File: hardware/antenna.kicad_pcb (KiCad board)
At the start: 2 copper layers, 9 parts, among them P1 CONN_01X05

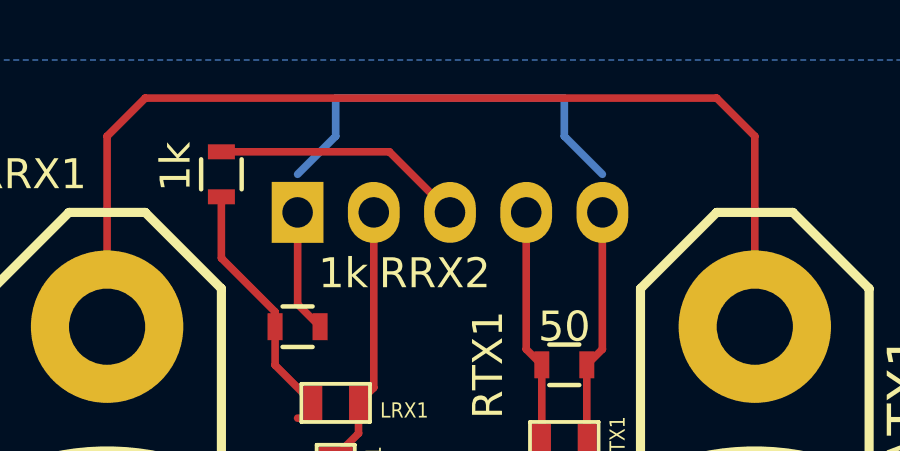
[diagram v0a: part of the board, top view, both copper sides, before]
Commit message: Fixing the ground plane fill.
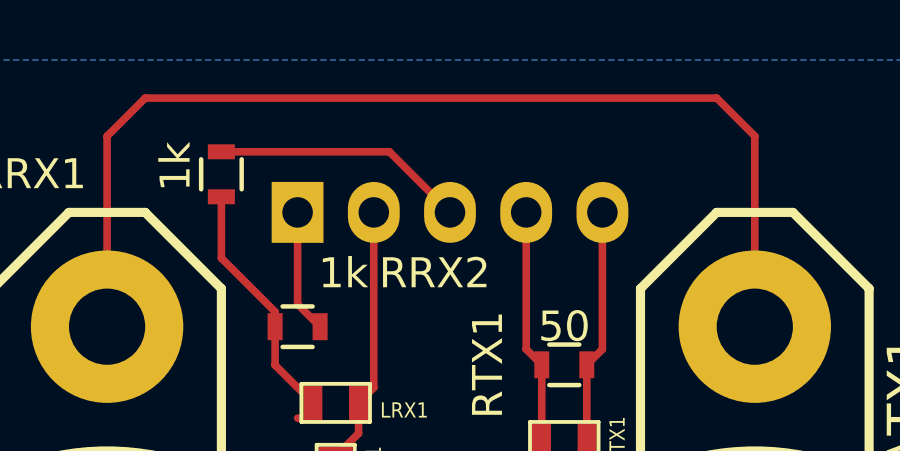
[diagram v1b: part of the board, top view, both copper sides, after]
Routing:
- net (no net): track 13.8 -> 0.00 mm
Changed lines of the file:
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@@
     (links 15)
     (no_connects 0)
-    (area 124.46 45.72 166.37 80.01)
+    (area 124.38608 45.72 165.100001 78.9432)
     (thickness 1.6)
     (drawings 0)
-    (tracks 37)
+    (tracks 32)
     (zones 0)
     (modules 9)
@@
     )
   )
-  (segment (start 139.7 49.53) (end 140.97 48.26) (width 0.254) (layer B.Cu) (net 0) (status 80010))
-  (segment (start 140.97 48.26) (end 140.97 46.99) (width 0.254) (layer B.Cu) (net 0) (status 80000))
-  (segment (start 140.97 46.99) (end 148.59 46.99) (width 0.254) (layer B.Cu) (net 0) (status 80000))
-  (segment (start 148.59 46.99) (end 148.59 48.26) (width 0.254) (layer B.Cu) (net 0) (status 80000))
-  (segment (start 148.59 48.26) (end 149.86 49.53) (width 0.254) (layer B.Cu) (net 0) (status 80020))
+  (segment (start 134.62 67.31) (end 134.62 64.262) (width 0.254) (layer F.Cu) (net 1))
+  (segment (start 140.208 60.452) (end 133.35 67.31) (width 0.254) (layer F.Cu) (net 1))
   (segment (start 140.97 60.452) (end 140.208 60.452) (width 0.254) (layer F.Cu) (net 1))
-  (segment (start 140.208 60.452) (end 133.35 67.31) (width 0.254) (layer F.Cu) (net 1))
-  (segment (start 134.62 67.31) (end 134.62 64.262) (width 0.254) (layer F.Cu) (net 1))
+  (segment (start 149.86 55.36) (end 149.34 55.88) (width 0.254) (layer F.Cu) (net 2))
+  (segment (start 149.86 50.8) (end 149.86 55.36) (width 0.254) (layer F.Cu) (net 2))
+  (segment (start 149.34 58.408) (end 149.352 58.42) (width 0.254) (layer F.Cu) (net 2))
+  (segment (start 149.34 55.88) (end 149.34 58.408) (width 0.254) (layer F.Cu) (net 2))
+  (segment (start 139.7 53.86) (end 140.45 54.61) (width 0.254) (layer F.Cu) (net 2))
+  (segment (start 139.7 50.8) (end 139.7 53.86) (width 0.254) (layer F.Cu) (net 2))
+  (segment (start 133.35 48.26) (end 134.62 46.99) (width 0.254) (layer F.Cu) (net 2))
+  (segment (start 134.62 46.99) (end 153.67 46.99) (width 0.254) (layer F.Cu) (net 2))
+  (segment (start 153.67 46.99) (end 154.94 48.26) (width 0.254) (layer F.Cu) (net 2))
+  (segment (start 154.94 48.26) (end 154.94 54.61) (width 0.254) (layer F.Cu) (net 2))
   (segment (start 133.35 54.61) (end 133.35 48.26) (width 0.254) (layer F.Cu) (net 2))
-  (segment (start 154.94 48.26) (end 154.94 54.61) (width 0.254) (layer F.Cu) (net 2))
-  (segment (start 153.67 46.99) (end 154.94 48.26) (width 0.254) (layer F.Cu) (net 2))
-  (segment (start 134.62 46.99) (end 153.67 46.99) (width 0.254) (layer F.Cu) (net 2))
-  (segment (start 133.35 48.26) (end 134.62 46.99) (width 0.254) (layer F.Cu) (net 2))
-  (segment (start 139.7 50.8) (end 139.7 53.86) (width 0.254) (layer F.Cu) (net 2))
-  (segment (start 139.7 53.86) (end 140.45 54.61) (width 0.254) (layer F.Cu) (net 2))
-  (segment (start 149.34 55.88) (end 149.34 58.408) (width 0.254) (layer F.Cu) (net 2))
-  (segment (start 149.34 58.408) (end 149.352 58.42) (width 0.254) (layer F.Cu) (net 2))
-  (segment (start 149.86 50.8) (end 149.86 55.36) (width 0.254) (layer F.Cu) (net 2))
-  (segment (start 149.86 55.36) (end 149.34 55.88) (width 0.254) (layer F.Cu) (net 2))
+  (segment (start 147.32 55.36) (end 147.84 55.88) (width 0.254) (layer F.Cu) (net 3))
+  (segment (start 147.32 50.8) (end 147.32 55.36) (width 0.254) (layer F.Cu) (net 3))
+  (segment (start 147.84 58.408) (end 147.828 58.42) (width 0.254) (layer F.Cu) (net 3))
+  (segment (start 147.84 55.88) (end 147.84 58.408) (width 0.254) (layer F.Cu) (net 3))
+  (segment (start 147.828 60.198) (end 154.94 67.31) (width 0.254) (layer F.Cu) (net 3))
   (segment (start 147.828 58.42) (end 147.828 60.198) (width 0.254) (layer F.Cu) (net 3))
-  (segment (start 147.828 60.198) (end 154.94 67.31) (width 0.254) (layer F.Cu) (net 3))
-  (segment (start 147.84 55.88) (end 147.84 58.408) (width 0.254) (layer F.Cu) (net 3))
-  (segment (start 147.84 58.408) (end 147.828 58.42) (width 0.254) (layer F.Cu) (net 3))
-  (segment (start 147.32 50.8) (end 147.32 55.36) (width 0.254) (layer F.Cu) (net 3))
-  (segment (start 147.32 55.36) (end 147.84 55.88) (width 0.254) (layer F.Cu) (net 3))
+  (segment (start 142.24 56.642) (end 141.732 57.15) (width 0.254) (layer F.Cu) (net 4))
+  (segment (start 142.24 50.8) (end 142.24 56.642) (width 0.254) (layer F.Cu) (net 4))
+  (segment (start 141.732 58.166) (end 140.97 58.928) (width 0.254) (layer F.Cu) (net 4))
   (segment (start 141.732 57.15) (end 141.732 58.166) (width 0.254) (layer F.Cu) (net 4))
-  (segment (start 141.732 58.166) (end 140.97 58.928) (width 0.254) (layer F.Cu) (net 4))
-  (segment (start 142.24 50.8) (end 142.24 56.642) (width 0.254) (layer F.Cu) (net 4))
-  (segment (start 142.24 56.642) (end 141.732 57.15) (width 0.254) (layer F.Cu) (net 4))
-  (segment (start 137.16 50.28) (end 137.16 52.324) (width 0.254) (layer F.Cu) (net 5) (status 400000))
-  (segment (start 138.95 54.114) (end 138.95 54.61) (width 0.254) (layer F.Cu) (net 5) (status 800000))
+  (segment (start 139.954 57.658) (end 139.7 57.658) (width 0.254) (layer F.Cu) (net 5))
+  (segment (start 138.95 55.892) (end 140.208 57.15) (width 0.254) (layer F.Cu) (net 5))
+  (segment (start 138.95 54.61) (end 138.95 55.892) (width 0.254) (layer F.Cu) (net 5))
   (segment (start 137.16 52.324) (end 138.95 54.114) (width 0.254) (layer F.Cu) (net 5))
-  (segment (start 138.95 54.61) (end 138.95 55.892) (width 0.254) (layer F.Cu) (net 5))
-  (segment (start 138.95 55.892) (end 140.208 57.15) (width 0.254) (layer F.Cu) (net 5))
-  (segment (start 139.954 57.658) (end 139.7 57.658) (width 0.254) (layer F.Cu) (net 5))
-  (segment (start 137.16 48.78) (end 142.76 48.78) (width 0.254) (layer F.Cu) (net 6) (status 400000))
-  (segment (start 142.76 48.78) (end 144.78 50.8) (width 0.254) (layer F.Cu) (net 6) (status 800000))
+  (segment (start 138.95 54.114) (end 138.95 54.61) (width 0.254) (layer F.Cu) (net 5))
+  (segment (start 137.16 50.28) (end 137.16 52.324) (width 0.254) (layer F.Cu) (net 5))
+  (segment (start 142.76 48.78) (end 144.78 50.8) (width 0.254) (layer F.Cu) (net 6))
+  (segment (start 137.16 48.78) (end 142.76 48.78) (width 0.254) (layer F.Cu) (net 6))
   (zone (net 2) (net_name AGND) (layer B.Cu) (hatch edge 0.508)
     (connect_pads (clearance 0.508))
